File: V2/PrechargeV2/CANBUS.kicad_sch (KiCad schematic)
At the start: 8 parts, among them J3 436500228, U7 MCP2551-I_SN, U8 MCP2515-I_SO, Y1 Crystal

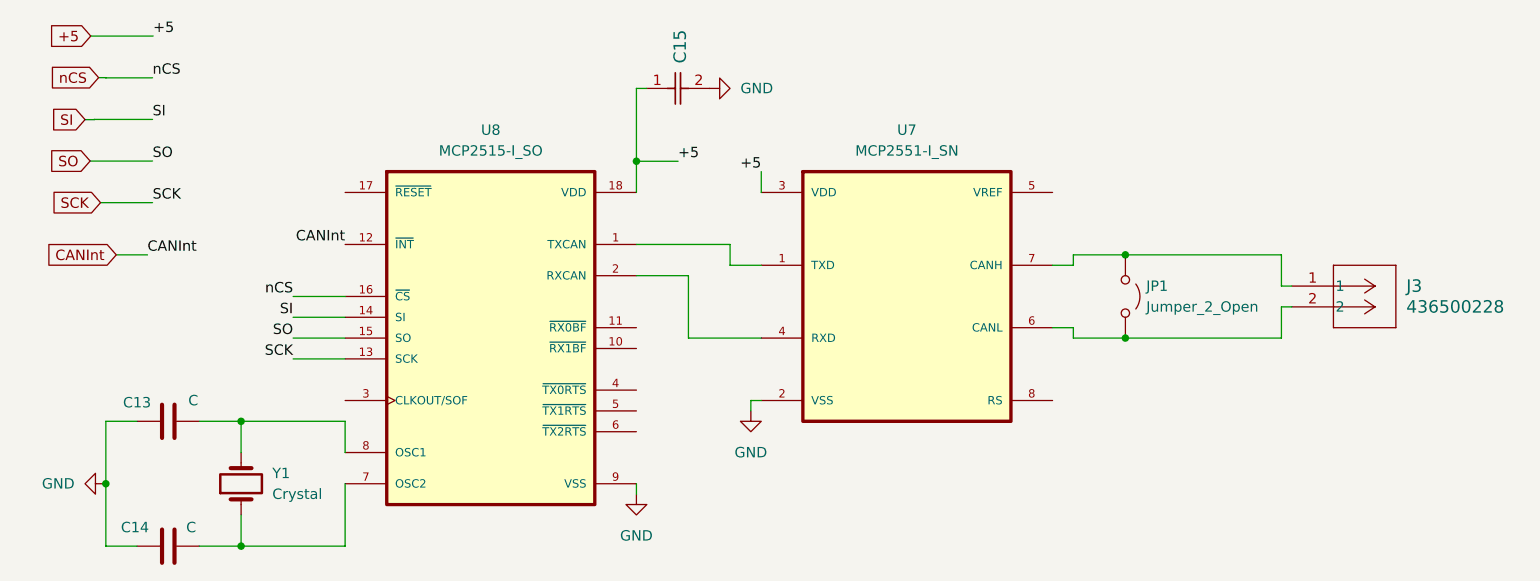
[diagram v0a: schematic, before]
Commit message: Updated Schematic For ESF
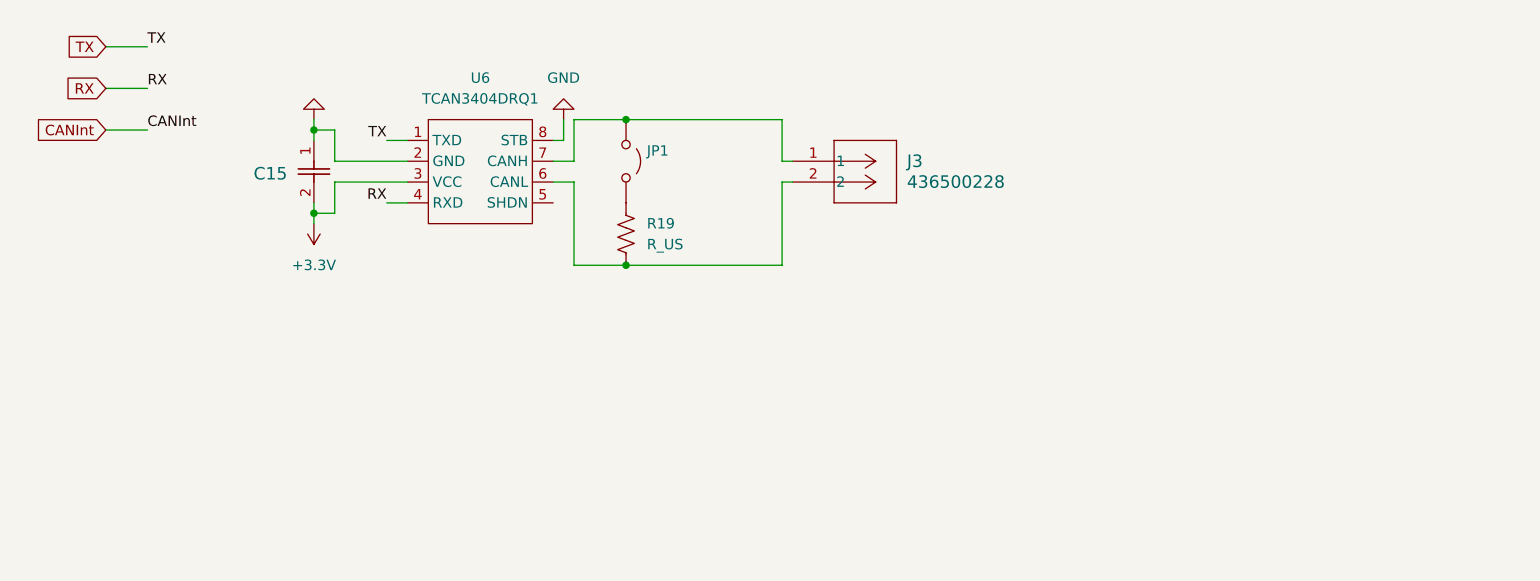
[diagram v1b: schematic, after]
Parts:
- removed C13, C14: C, Capacitor_THT:C_Disc_D3.8mm_W2.6mm_P2.50mm, symbol Device:C
- removed U7: MCP2551-I_SN, CANBUS:SOIC127P599X175-8N, symbol MCP2551-I_SN:MCP2551-I_SN
- removed U8: MCP2515-I_SO, CANBUS:SOIC127P1030X265-18N, symbol MCP2515-I_SO:MCP2515-I_SO
- removed Y1: Crystal, Crystal:Crystal_HC49-U_Vertical, symbol Device:Crystal
- added R19: R_US, symbol Device:R_US
- added U6: TCAN3404DRQ1, Package_TO_SOT_SMD:SOT-23-8, symbol TCAN:TCAN3404DRQ1
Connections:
- net +5 is gone; now on net GND: C15.1
- net GND: now also U6.2 (GND), U6.8 (STB); no longer C15.2
- net at JP1.2 (B): now also R19.1; no longer J3.2
- net at J3.1, JP1.1 (A): now also U6.7 (CANH)
- new net: J3.2, R19.2, U6.6 (CANL)
- new net +3.3V: C15.2, U6.3 (VCC)
- new net RX: U6.4 (RXD)
- new net TX: U6.1 (TXD)
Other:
- moved on the sheet: C15, J3, JP1
